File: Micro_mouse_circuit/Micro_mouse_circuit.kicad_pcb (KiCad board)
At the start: 2 copper layers, 3 parts, among them J1 Conn_02x16_Odd_Even, U1 HUSB237-AA001-DN06R, U2 SK22D15L5

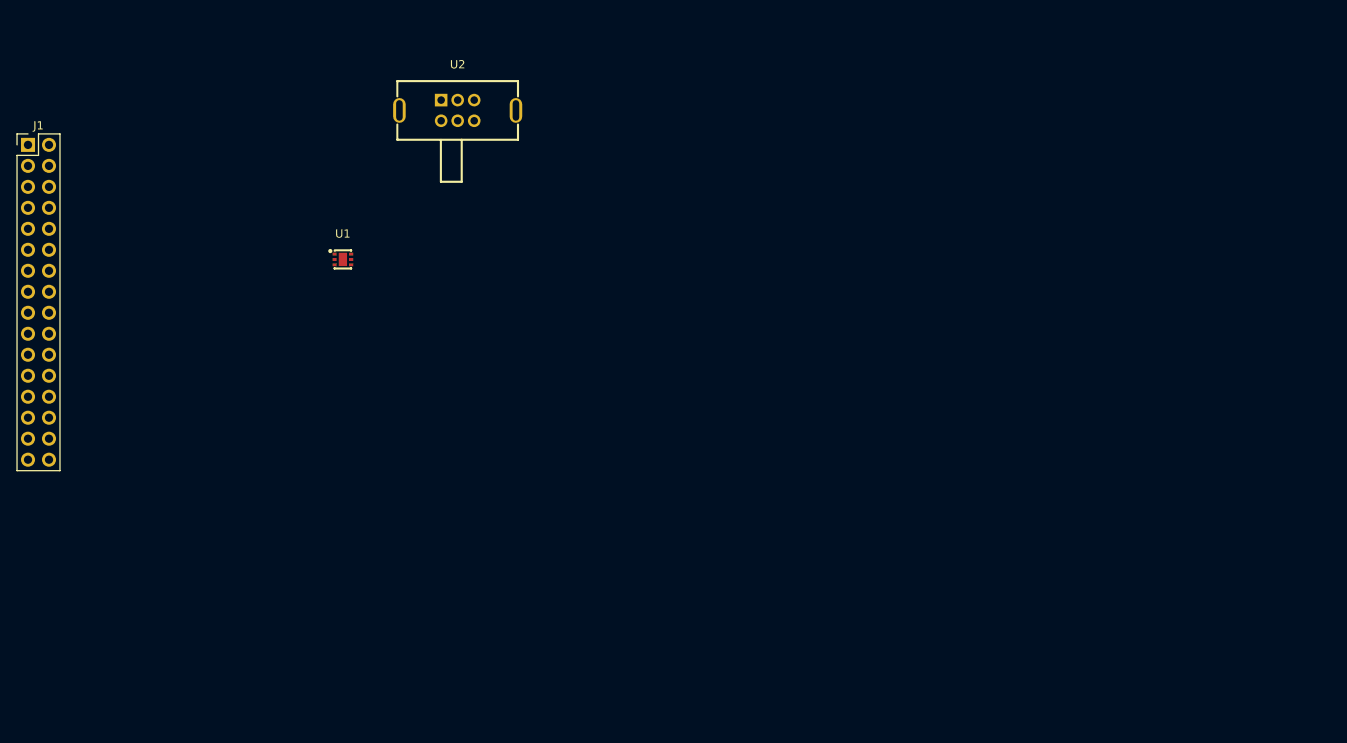
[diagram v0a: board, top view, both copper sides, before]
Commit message: adding footprint libraries
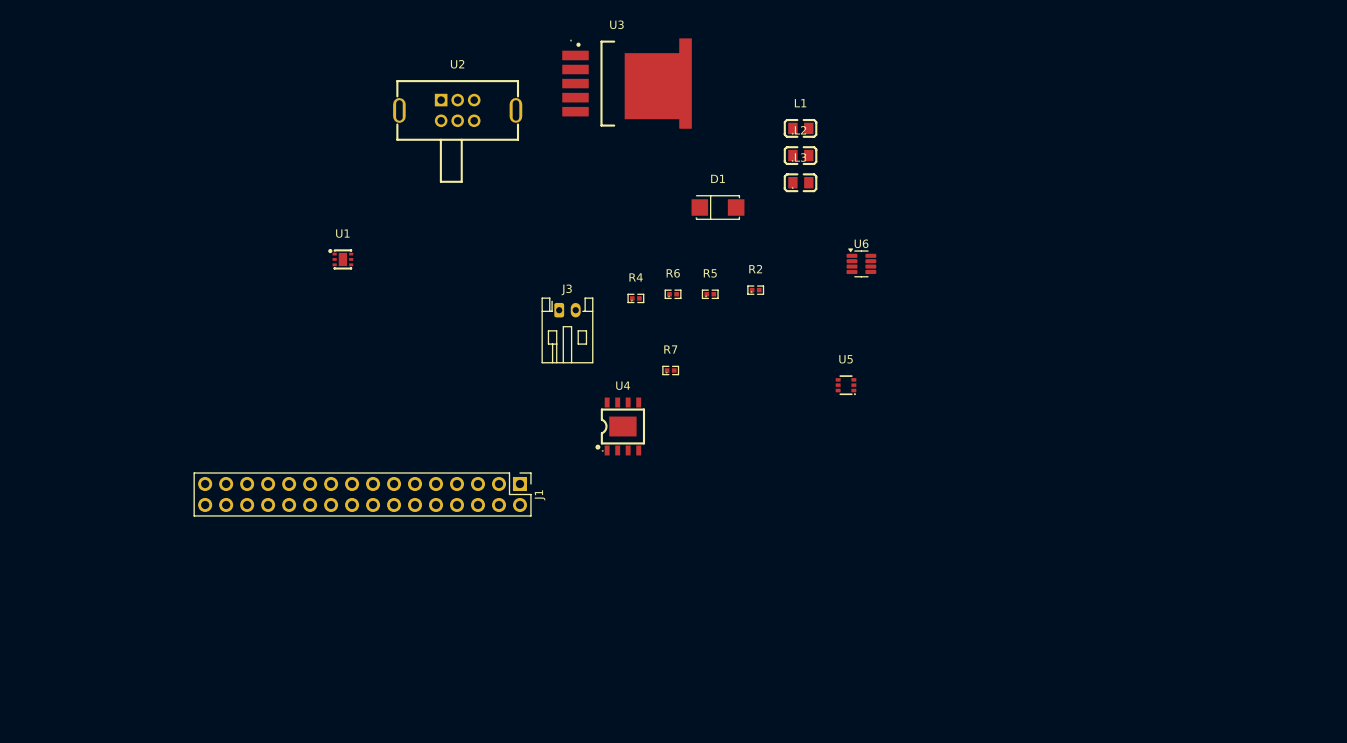
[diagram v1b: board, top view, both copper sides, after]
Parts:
- added D1: SS34_C8678, xxcustom_footprint:SMA_L4.3-W2.6-LS5.2-RD, F.Cu at (189.5, 75.5)
- added J3: Conn_01x02, Connector_JST:JST_PH_S2B-PH-K_1x02_P2.00mm_Horizontal, F.Cu at (170.3, 87.9)
- added L1: 10uH, xxcustom_footprint:L0805, F.Cu at (199.5, 65.9)
- added L2: 10uH, xxcustom_footprint:L0805, F.Cu at (199.5, 69.2)
- added L3: 10uH, xxcustom_footprint:L0805, F.Cu at (199.5, 72.5)
- added R2: 2k, xxcustom_footprint:R0402, F.Cu at (194.1, 85.5)
- added R4: 1k, xxcustom_footprint:R0402, F.Cu at (179.6, 86.5)
- added R5: 1k, xxcustom_footprint:R0402, F.Cu at (188.6, 86.0)
- added R6: 2k, xxcustom_footprint:R0402, F.Cu at (184.1, 86.0)
- added R7: 6k, xxcustom_footprint:R0402, F.Cu at (183.8, 95.2)
- added U3: LM2596SX-5_0/NOPB, xxcustom_footprint:TO-263-5_L10.2-W8.9-P1.70-TL, F.Cu at (177.3, 60.5)
- added U4: TP4056_C382139, xxcustom_footprint:ESOP-8_L4.9-W3.9-P1.27-LS6.0-BL-EP, F.Cu at (178.0, 102.0)
- added U5: SN74LVC1G3157DCKR, xxcustom_footprint:SC-70-6_L2.2-W1.3-P0.65-LS2.1-BR, F.Cu at (205.0, 97.0)
- added U6: INA219AxDCN, Package_TO_SOT_SMD:SOT-23-8, F.Cu at (206.9, 82.3)
- moved J1 72.3 mm to (165.5, 109.0), turned to -90 degrees
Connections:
- J1 pad 14: /Battery -> Battery
- U2 pad 1: 9V -> 9V_in

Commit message: assigned additional footprints
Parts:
- added R8: 0.2A, xxcustom_footprint:R2512, F.Cu at (176.4, 104.0)
- moved U2 63.1 mm to (116.5, 111.2)
- moved L1 47.0 mm to (152.5, 64.4)
- moved L2 47.0 mm to (152.5, 67.7)
- moved L3 47.0 mm to (152.5, 71.0)
- moved U6 35.1 mm to (176.0, 99.0)
- moved D1 31.3 mm to (158.5, 80.0)
- moved U1 27.0 mm to (124.0, 99.9)
- moved J3 22.1 mm to (175.0, 109.5)
- moved U4 18.1 mm to (164.0, 90.5)
- moved U3 8.47 mm to (172.5, 67.5)

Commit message: 02/28 submission
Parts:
- moved U1 98.1 mm to (219.5, 122.2)
- moved D1 82.3 mm to (240.5, 87.6)
- moved L1 82.3 mm to (234.5, 72.0)
- moved L2 82.3 mm to (234.5, 75.3)
- moved L3 82.3 mm to (234.5, 78.6)
- moved U3 82.3 mm to (254.5, 75.1)
- moved U4 82.3 mm to (246.0, 98.1)
- moved U2 81.6 mm to (196.0, 129.5)
- moved R6 46.7 mm to (230.6, 90.5)
- moved R7 46.7 mm to (230.3, 99.7)
- moved J3 45.6 mm to (220.4, 113.7)
- moved R8 45.6 mm to (221.8, 108.2)
- moved U6 45.6 mm to (221.4, 103.2)
- moved R4 44.1 mm to (223.1, 79.5)
- moved U5 32.8 mm to (237.6, 93.0)
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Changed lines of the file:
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@@
 	(footprint "Package_TO_SOT_SMD:SOT-23-8"
 		(layer "F.Cu")
-		(at 176 99)
+		(at 221.3625 103.175)
 		(descr "SOT, 8 Pin (JEDEC MO-178 Var BA https://www.jedec.org/document_search?search_api_views_fulltext=MO-178), generated with kicad-footprint-generator ipc_gullwing_generator.py")
 		(tags "SOT TO_SOT_SMD")
@@
 	(footprint "xxcustom_footprint:L0805"
 		(layer "F.Cu")
-		(at 152.533782 67.713996)
+		(at 234.533782 75.286004)
 		(descr "L0805 footprint")
 		(tags "L0805 footprint C1046")
@@
 	(footprint "xxcustom_footprint:SW-TH_XKB_SK22D15L7"
 		(layer "F.Cu")
-		(at 116.5 111.249936)
+		(at 196 129.5)
 		(descr "SW-TH_XKB_SK22D15L7 footprint")
 		(tags "SW-TH_XKB_SK22D15L7 footprint C2884795")
@@
 	(footprint "xxcustom_footprint:SC-70-6_L2.2-W1.3-P0.65-LS2.1-BR"
 		(layer "F.Cu")
-		(at 205 97)
+		(at 237.550038 93)
 		(descr "SC-70-6_L2.2-W1.3-P0.65-LS2.1-BR footprint")
 		(tags "SC-70-6_L2.2-W1.3-P0.65-LS2.1-BR footprint C38663")
@@
 	(footprint "xxcustom_footprint:R0402"
 		(layer "F.Cu")
-		(at 184.067183 86)
+		(at 230.567183 90.5)
 		(descr "R0402 footprint")
 		(tags "R0402 footprint C4109")
@@
 	(footprint "xxcustom_footprint:ESOP-8_L4.9-W3.9-P1.27-LS6.0-BL-EP"
 		(layer "F.Cu")
-		(at 164 90.5)
+		(at 246 98.072008)
 		(descr "ESOP-8_L4.9-W3.9-P1.27-LS6.0-BL-EP footprint")
 		(tags "ESOP-8_L4.9-W3.9-P1.27-LS6.0-BL-EP footprint C382139")
@@
 	(footprint "xxcustom_footprint:R0402"
 		(layer "F.Cu")
-		(at 179.567183 86.5)
+		(at 223.134366 79.5)
 		(descr "R0402 footprint")
 		(tags "R0402 footprint C4109")
@@
 		)
 		(fp_text user "REF**"
-			(at 0 4.498603 0)
+			(at 45.3625 8.673603 0)
 			(layer "F.Fab")
 			(effects
@@
 	(footprint "xxcustom_footprint:R0402"
 		(layer "F.Cu")
-		(at 188.567183 86)
+		(at 218.067183 80)
 		(descr "R0402 footprint")
 		(tags "R0402 footprint C4109")
@@
 	(footprint "xxcustom_footprint:R0402"
 		(layer "F.Cu")
-		(at 183.780523 95.22324)
+		(at 230.280523 99.72324)
 		(descr "R0402 footprint")
 		(tags "R0402 footprint C4109")
@@
 	(footprint "Connector_JST:JST_PH_S2B-PH-K_1x02_P2.00mm_Horizontal"
 		(layer "F.Cu")
-		(at 175 109.5)
+		(at 220.3625 113.675)
 		(descr "JST PH series connector, S2B-PH-K (http://www.jst-mfg.com/product/pdf/eng/ePH.pdf), generated with kicad-footprint-generator")
 		(tags "connector JST PH top entry")
@@
 	(footprint "xxcustom_footprint:TO-263-5_L10.2-W8.9-P1.70-TL"
 		(layer "F.Cu")
-		(at 172.5 67.5)
+		(at 254.5 75.072008)
 		(descr "TO-263-5_L10.2-W8.9-P1.70-TL footprint")
 		(tags "TO-263-5_L10.2-W8.9-P1.70-TL footprint C10002")
@@
 	(footprint "xxcustom_footprint:SMA_L4.3-W2.6-LS5.2-RD"
 		(layer "F.Cu")
-		(at 158.5 80)
+		(at 240.5 87.572008)
 		(descr "SMA_L4.3-W2.6-LS5.2-RD footprint")
 		(tags "SMA_L4.3-W2.6-LS5.2-RD footprint C8678")
@@
 	(footprint "xxcustom_footprint:L0805"
 		(layer "F.Cu")
-		(at 152.533782 64.427992)
+		(at 234.533782 72)
 		(descr "L0805 footprint")
 		(tags "L0805 footprint C1046")
@@
 	(footprint "xxcustom_footprint:L0805"
 		(layer "F.Cu")
-		(at 152.533782 71)
+		(at 234.533782 78.572008)
 		(descr "L0805 footprint")
 		(tags "L0805 footprint C1046")
@@
 	(footprint "xxcustom_footprint:TDFN-6_L2.0-W2.0-P0.65-TL-EP"
 		(layer "F.Cu")
-		(at 123.999924 99.850038)
+		(at 219.499924 122.150013)
 		(descr "TDFN-6_L2.0-W2.0-P0.65-TL-EP footprint")
 		(tags "TDFN-6_L2.0-W2.0-P0.65-TL-EP footprint C22373734")
@@
 		)
 		(property "Value" "HUSB237-AA001-DN06R"
-			(at -0.007963 3.099975 0)
+			(at 79.492037 21.350039 0)
 			(layer "F.Fab")
 			(effects
@@
 	(footprint "xxcustom_footprint:R0402"
 		(layer "F.Cu")
-		(at 194.067183 85.5)
+		(at 223.567183 79.5)
 		(descr "R0402 footprint")
 		(tags "R0402 footprint C4109")
@@
 	(footprint "xxcustom_footprint:R2512"
 		(layer "F.Cu")
-		(at 176.433706 104)
+		(at 221.796206 108.175)
 		(descr "R2512 footprint")
 		(tags "R2512 footprint C459674")
